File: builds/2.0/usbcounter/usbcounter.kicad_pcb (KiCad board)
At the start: 2 copper layers, 64 x 48.8 mm, 39 parts, among them IC1 ATTINY826-XUR, J1 UJ2-MIBH-G-SMT-TR, J2 Conn_IN, J3 Conn_Prog, J4 Conn_Disp, U1 MCP23008-xSO, U2 FT230XS, U3 74LV8154, U4 MCP23008-xSO, U5 NCP1117 3.3V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

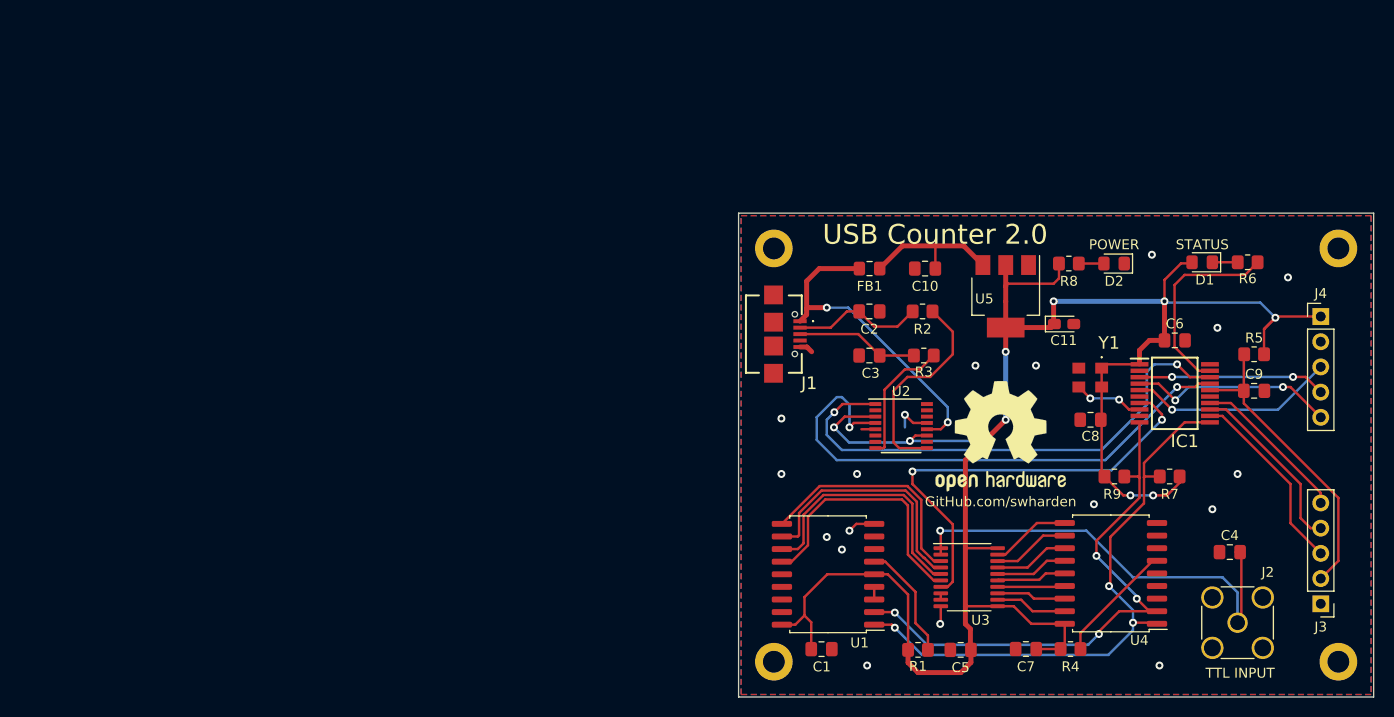
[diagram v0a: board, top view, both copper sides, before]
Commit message: 2.0: reset PCB
using JLCPCB rules
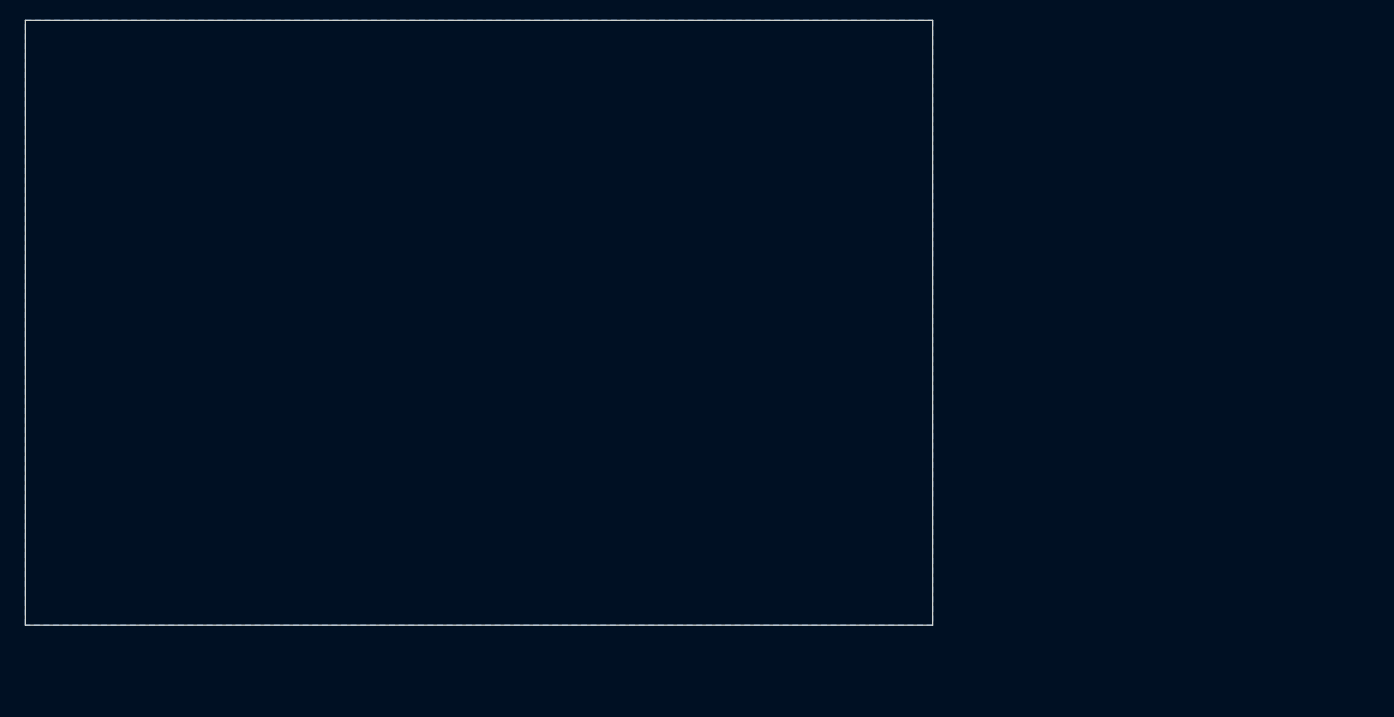
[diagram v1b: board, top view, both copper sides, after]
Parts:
- removed C1, C10, C5, C6, C7, C8, C9: .1u, Capacitor_SMD:C_0805_2012Metric_Pad1.18x1.45mm_HandSolder
- removed C11: .1u, Capacitor_Tantalum_SMD:CP_EIA-2012-15_AVX-P_Pad1.30x1.05mm_HandSolder
- removed C2, C3: 47p, Capacitor_SMD:C_0805_2012Metric_Pad1.18x1.45mm_HandSolder
- removed C4: 50, Capacitor_SMD:C_0805_2012Metric_Pad1.18x1.45mm_HandSolder
- removed D1: STATUS, LED_SMD:LED_0805_2012Metric_Pad1.15x1.40mm_HandSolder
- removed D2: POWER, LED_SMD:LED_0805_2012Metric_Pad1.15x1.40mm_HandSolder
- removed FB1: Ferrite, Inductor_SMD:L_0805_2012Metric_Pad1.15x1.40mm_HandSolder
- removed H1, H2, H3, H4: Hole, MountingHole:MountingHole_2.2mm_M2_DIN965_Pad
- removed IC1: ATTINY826-XUR, Library Loader:SOP65P780X200-20N
- removed J1: UJ2-MIBH-G-SMT-TR, Library Loader:UJ2MIBHGSMTTR
- removed J2: Conn_IN, Connector_Coaxial:SMA_Amphenol_132291_Vertical
- removed J3: Conn_Prog, Connector_PinHeader_2.54mm:PinHeader_1x05_P2.54mm_Vertical
- removed J4: Conn_Disp, Connector_PinHeader_2.54mm:PinHeader_1x05_P2.54mm_Vertical
- removed R1, R4, R5, R6, R7, R8, R9: 10k, Resistor_SMD:R_0805_2012Metric_Pad1.20x1.40mm_HandSolder
- removed R2, R3: 27, Resistor_SMD:R_0805_2012Metric_Pad1.20x1.40mm_HandSolder
- removed REF**: OSHW-Logo2_14.6x12mm_SilkScreen, Symbol:OSHW-Logo2_14.6x12mm_SilkScreen
- removed U1, U4: MCP23008-xSO, Package_SO:SOIC-18W_7.5x11.6mm_P1.27mm
- removed U2: FT230XS, Package_SO:SSOP-16_3.9x4.9mm_P0.635mm
- removed U3: 74LV8154, Package_SO:TSSOP-20_4.4x6.5mm_P0.65mm
- removed U5: NCP1117 3.3V, Package_TO_SOT_SMD:SOT-223-3_TabPin2
- removed Y1: 14.7456 MHz TCXO, Library Loader:ECSTXO3225MV1474TR
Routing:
- net VCC: track 207.7 -> 0.00 mm, vias 9 -> 0
- net SCL: track 60.1 -> 0.00 mm, vias 3 -> 0
- net SDA: track 56.8 -> 0.00 mm, vias 4 -> 0
- net PCRX: track 55.6 -> 0.00 mm, vias 2 -> 0
- net PCTX: track 52.4 -> 0.00 mm, vias 2 -> 0
- net Net-(C4-Pad2): track 45.5 -> 0.00 mm, vias 1 -> 0
- net GATE: track 44.8 -> 0.00 mm, vias 2 -> 0
- net 5V: track 32.5 -> 0.00 mm, vias 2 -> 0
- net RST: track 30.7 -> 0.00 mm
- net Net-(U1-Pad13): track 26.6 -> 0.00 mm
- net Net-(U1-Pad12): track 26.1 -> 0.00 mm
- net Net-(U1-Pad11): track 25.4 -> 0.00 mm
- net Net-(U1-Pad10): track 23.6 -> 0.00 mm
- net Net-(R2-Pad2): track 21.5 -> 0.00 mm
- net DISP_DAT: track 20.9 -> 0.00 mm, vias 1 -> 0
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- removed copper zone on F.Cu, net GND
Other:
- board size 64 x 48.8 mm -> 91.4 x 61 mm
- board text removed: "GitHub.com/swharden"
- board text removed: "POWER"
- board text removed: "STATUS"
- board text removed: "TTL INPUT"
- board text removed: "USB Counter 2.0"

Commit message: 3.0: new board
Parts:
- added C1: .1u, Capacitor_SMD:C_0805_2012Metric_Pad1.18x1.45mm_HandSolder, F.Cu at (95.5, 65.0)
- added C10: .1u, Capacitor_SMD:C_0805_2012Metric_Pad1.18x1.45mm_HandSolder, F.Cu at (60.8, 58.3)
- added C11: .1u, Capacitor_Tantalum_SMD:CP_EIA-2012-15_AVX-P_Pad1.30x1.05mm_HandSolder, F.Cu at (71.0, 63.3)
- added C12: .1u, Capacitor_SMD:C_0805_2012Metric_Pad1.18x1.45mm_HandSolder, F.Cu at (130.3, 87.9)
- added C2: 47p, Capacitor_SMD:C_0805_2012Metric_Pad1.18x1.45mm_HandSolder, F.Cu at (61.6, 70.0)
- added C3: 47p, Capacitor_SMD:C_0805_2012Metric_Pad1.18x1.45mm_HandSolder, F.Cu at (61.6, 74.3)
- added C4: .1u, Capacitor_SMD:C_0805_2012Metric_Pad1.18x1.45mm_HandSolder, F.Cu at (81.4, 98.4)
- added C5: .1u, Capacitor_SMD:C_0805_2012Metric_Pad1.18x1.45mm_HandSolder, F.Cu at (90.7, 100.1)
- added C6: .1u, Capacitor_SMD:C_0805_2012Metric_Pad1.18x1.45mm_HandSolder, F.Cu at (103.6, 65.0)
- added C7: .1u, Capacitor_SMD:C_0805_2012Metric_Pad1.18x1.45mm_HandSolder, F.Cu at (118.1, 91.4)
- added C8: .1u, Capacitor_SMD:C_0805_2012Metric_Pad1.18x1.45mm_HandSolder, F.Cu at (93.2, 77.0)
- added C9: .1u, Capacitor_SMD:C_0805_2012Metric_Pad1.18x1.45mm_HandSolder, F.Cu at (99.3, 99.1)
- added D1: STATUS, LED_SMD:LED_0805_2012Metric_Pad1.15x1.40mm_HandSolder, F.Cu at (105.9, 62.7)
- added D2: D, Diode_SMD:D_SOD-323_HandSoldering, F.Cu at (81.0, 95.9)
- added D3: D, Diode_SMD:D_SOD-323_HandSoldering, F.Cu at (81.0, 101.0)
- added D4: POWER, LED_SMD:LED_0805_2012Metric_Pad1.15x1.40mm_HandSolder, F.Cu at (73.3, 58.5)
- added FB1: Ferrite, Inductor_SMD:L_0805_2012Metric_Pad1.15x1.40mm_HandSolder, F.Cu at (57.5, 64.1)
- added H1: Hole, MountingHole:MountingHole_2.2mm_M2_DIN965_Pad, F.Cu at (54.6, 54.6)
- added H2: Hole, MountingHole:MountingHole_2.2mm_M2_DIN965_Pad, F.Cu at (138.4, 54.6)
- added H3: Hole, MountingHole:MountingHole_2.2mm_M2_DIN965_Pad, F.Cu at (54.6, 108.0)
- added H4: Hole, MountingHole:MountingHole_2.2mm_M2_DIN965_Pad, F.Cu at (138.4, 108.0)
- added IC1: ATTINY826-XUR, Library Loader:SOP65P780X200-20N, F.Cu at (101.1, 70.4)
- added J1: UJ2-MIBH-G-SMT-TR, Library Loader:UJ2MIBHGSMTTR, F.Cu at (54.6, 72.5)
- added J2: SMA, Connector_Coaxial:SMA_Amphenol_901-144_Vertical, F.Cu at (57.9, 97.5)
- added J3: Conn_Prog, Connector_PinHeader_2.54mm:PinHeader_1x05_P2.54mm_Vertical, F.Cu at (125.5, 54.1)
- added J4: Conn_Disp, Connector_PinHeader_2.54mm:PinHeader_1x05_P2.54mm_Vertical, F.Cu at (138.4, 64.5)
- added JP1: Jumper, Connector_PinHeader_2.54mm:PinHeader_1x03_P2.54mm_Vertical, F.Cu at (73.4, 95.2)
- added Q1: MMBT2222A, Package_TO_SOT_SMD:SOT-23, F.Cu at (86.7, 99.7)
- added R1: 50, Resistor_THT:R_Axial_DIN0207_L6.3mm_D2.5mm_P10.16mm_Horizontal, F.Cu at (64.3, 106.2)
- added R10: 10k, Resistor_SMD:R_0805_2012Metric_Pad1.20x1.40mm_HandSolder, F.Cu at (81.0, 93.3)
- added R11: 10k, Resistor_SMD:R_0805_2012Metric_Pad1.20x1.40mm_HandSolder, F.Cu at (88.6, 95.0)
- added R12: 10k, Resistor_SMD:R_0805_2012Metric_Pad1.20x1.40mm_HandSolder, F.Cu at (102.4, 95.5)
- added R13: 10k, Resistor_SMD:R_0805_2012Metric_Pad1.20x1.40mm_HandSolder, F.Cu at (118.1, 96.0)
- added R14: 10k, Resistor_SMD:R_0805_2012Metric_Pad1.20x1.40mm_HandSolder, F.Cu at (73.3, 63.3)
- added R2: 10k, Resistor_SMD:R_0805_2012Metric_Pad1.20x1.40mm_HandSolder, F.Cu at (99.6, 65.0)
- added R3: 100k, Resistor_SMD:R_0805_2012Metric_Pad1.20x1.40mm_HandSolder, F.Cu at (77.2, 95.9)
- added R4: 10k, Resistor_SMD:R_0805_2012Metric_Pad1.20x1.40mm_HandSolder, F.Cu at (109.0, 63.8)
- added R5: 27, Resistor_SMD:R_0805_2012Metric_Pad1.20x1.40mm_HandSolder, F.Cu at (64.1, 70.0)
- added R6: 27, Resistor_SMD:R_0805_2012Metric_Pad1.20x1.40mm_HandSolder, F.Cu at (64.1, 74.3)
- added R7: 10k, Resistor_SMD:R_0805_2012Metric_Pad1.20x1.40mm_HandSolder, F.Cu at (106.2, 78.2)
- added R8: 100k, Resistor_SMD:R_0805_2012Metric_Pad1.20x1.40mm_HandSolder, F.Cu at (85.5, 94.9)
- added R9: 10k, Resistor_SMD:R_0805_2012Metric_Pad1.20x1.40mm_HandSolder, F.Cu at (101.9, 78.2)
- added U1: FT230XS, Package_SO:SSOP-16_3.9x4.9mm_P0.635mm, F.Cu at (71.5, 73.5)
- added U2: SN74LVC1Gxx, Package_TO_SOT_SMD:SOT-23-5, F.Cu at (92.7, 96.0)
- added U3: MCP23008-xSO, Package_SO:SOIC-18W_7.5x11.6mm_P1.27mm, F.Cu at (110.0, 95.5)
- added U4: 74LV8154, Package_SO:TSSOP-20_4.4x6.5mm_P0.65mm, F.Cu at (96.8, 104.1)
- added U5: NCP1117 3.3V, Package_TO_SOT_SMD:SOT-223-3_TabPin2, F.Cu at (66.2, 60.8)
- added U6: MCP23008-xSO, Package_SO:SOIC-18W_7.5x11.6mm_P1.27mm, F.Cu at (126.2, 95.5)
- added Y1: 14.7456 MHz TCXO, Library Loader:ECSTXO3225MV1474TR, F.Cu at (93.2, 73.2)
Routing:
- net GND: track 0.00 -> 65.5 mm, vias 0 -> 32
- net PCTX: track 0.00 -> 52.9 mm, vias 0 -> 2
- net PCRX: track 0.00 -> 51.9 mm, vias 0 -> 2
- net Net-(U4-Pad12): track 0.00 -> 50.3 mm
- net VCC: track 0.00 -> 50.3 mm
- net Net-(U4-Pad13): track 0.00 -> 48.1 mm
- net Net-(U4-Pad14): track 0.00 -> 45.9 mm
- net SDA: track 0.00 -> 45.2 mm, vias 0 -> 2
- net RST: track 0.00 -> 43.9 mm
- net DISP_CLK: track 0.00 -> 43.8 mm, vias 0 -> 1
- net Net-(U4-Pad15): track 0.00 -> 43.4 mm
- net DISP_CS: track 0.00 -> 42.3 mm, vias 0 -> 1
- net DISP_DAT: track 0.00 -> 41.7 mm, vias 0 -> 1
- net Net-(U4-Pad16): track 0.00 -> 41.1 mm
- net SCL: track 0.00 -> 39.1 mm
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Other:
- board text added: "Display"
- board text added: "Harden Technologies, LLC"
- board text added: "Programmer"
- board text added: "RF"
- board text added: "TTL"
- board text added: "Termination Load"
- board text added: "USB Counter"
- board text added: "v3r1"

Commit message: 2.0: improve layout
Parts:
- moved C1 16.4 mm to (111.3, 60.5)
- moved D4 16.3 mm to (89.2, 54.9), turned to 180 degrees
- moved R14 14.5 mm to (85.1, 54.9), turned to 180 degrees
- moved R2 11.9 mm to (111.3, 62.7), turned to 180 degrees
- moved R4 9.67 mm to (105.2, 54.9), turned to 0 degrees
- moved D1 9.24 mm to (101.1, 54.9)
- moved C11 8.54 mm to (79.2, 61.2)
- moved C10 8.54 mm to (69.1, 56.1), turned to -90 degrees
- moved U5 8.54 mm to (74.4, 58.7)
- moved C6 7.39 mm to (96.2, 65.3), turned to 180 degrees
- moved U1 4.86 mm to (75.7, 75.9)
- moved C3 1.83 mm to (62.7, 75.7), turned to 180 degrees
- moved C2 1.79 mm to (62.7, 68.6), turned to 180 degrees
- moved R5 1.67 mm to (62.7, 70.9), turned to 0 degrees
- moved R6 1.63 mm to (62.7, 73.4), turned to 180 degrees
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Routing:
- net VCC: track 50.3 -> 303.7 mm, vias 0 -> 15
- net PCTX: track 52.9 -> 38.2 mm
- net GND: track 65.5 -> 51.1 mm
- net Net-(R6-Pad1): track 4.96 -> 19.1 mm
- net PCRX: track 51.9 -> 39.4 mm
- net Net-(C10-Pad1): track 11.1 -> 19.7 mm
- net STATUS: track 6.61 -> 15.0 mm
- net RST: track 43.9 -> 36.2 mm
- net Net-(R5-Pad2): track 15.2 -> 19.7 mm
- net 5V: track 34.3 -> 32.7 mm, vias 2 -> 0
- net Net-(D4-Pad2): track 2.80 -> 2.06 mm
- net DISP_CLK: track 43.8 -> 44.6 mm
- net OVF: track 0.00 -> 0.65 mm
- net DISP_DAT: track 41.7 -> 42.4 mm
- net Net-(C5-Pad2): vias 1 -> 0
- added copper zone on F.Cu, net 5V
- added copper zone on F.Cu, net GND
- added copper zone on F.Cu, net VCC
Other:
- board size 91.4 x 61 mm -> 91.4 x 60.9 mm
- board text added: "JLCJLCJLCJLC"
- board text added: "Power"
- board text added: "Status"
- board text added: "v2.1 @swharden"
- board text removed: "Harden Technologies, LLC"
- board text removed: "v3r1"
